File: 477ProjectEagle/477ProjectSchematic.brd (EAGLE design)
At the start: 101.6 x 76.2 mm, 67 parts, among them J1 POWER_JACK_BAT, J2 POWER_JACK_12VOUT, Q1 AO4419, X1 22-23-2051, X10 22-23-2041, X2 XRJK-S-01-6-6-0-2G2-NO

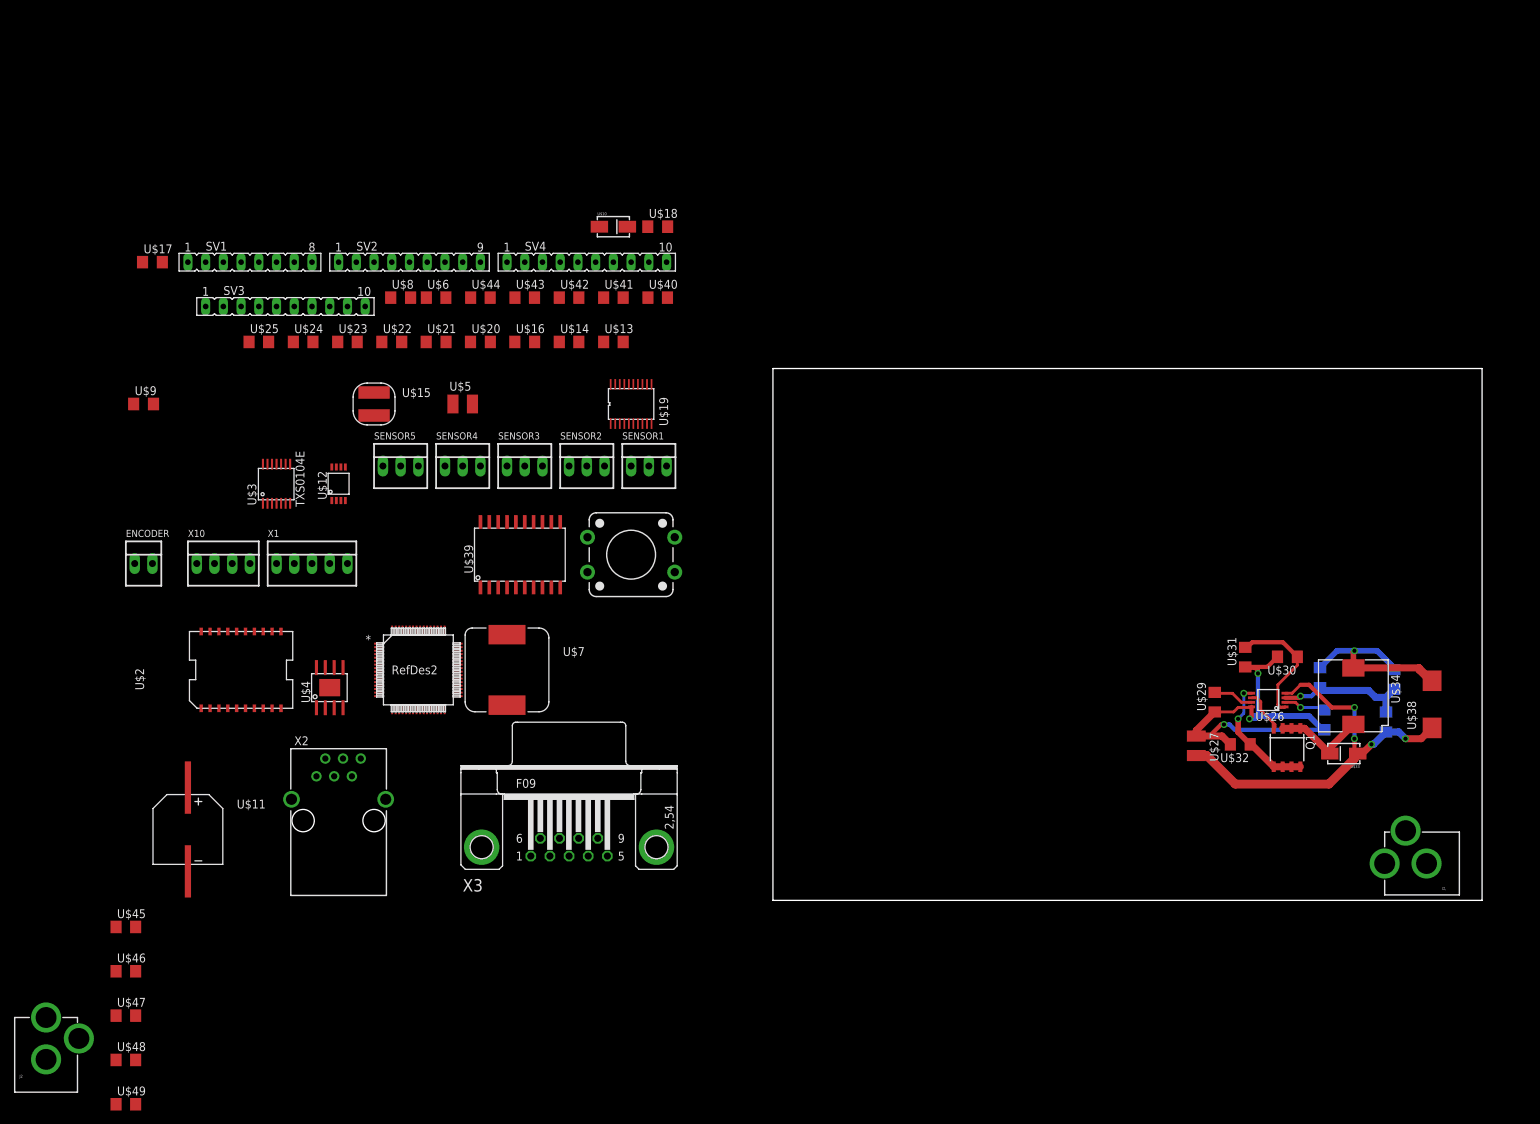
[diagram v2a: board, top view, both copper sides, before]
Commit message: More work on main PCB
Fixed some trace sizes on 12V power supply. Fixed some library
components to be the right size (Cout for the 7V power supply). Started
laying out 7V power supply circuit
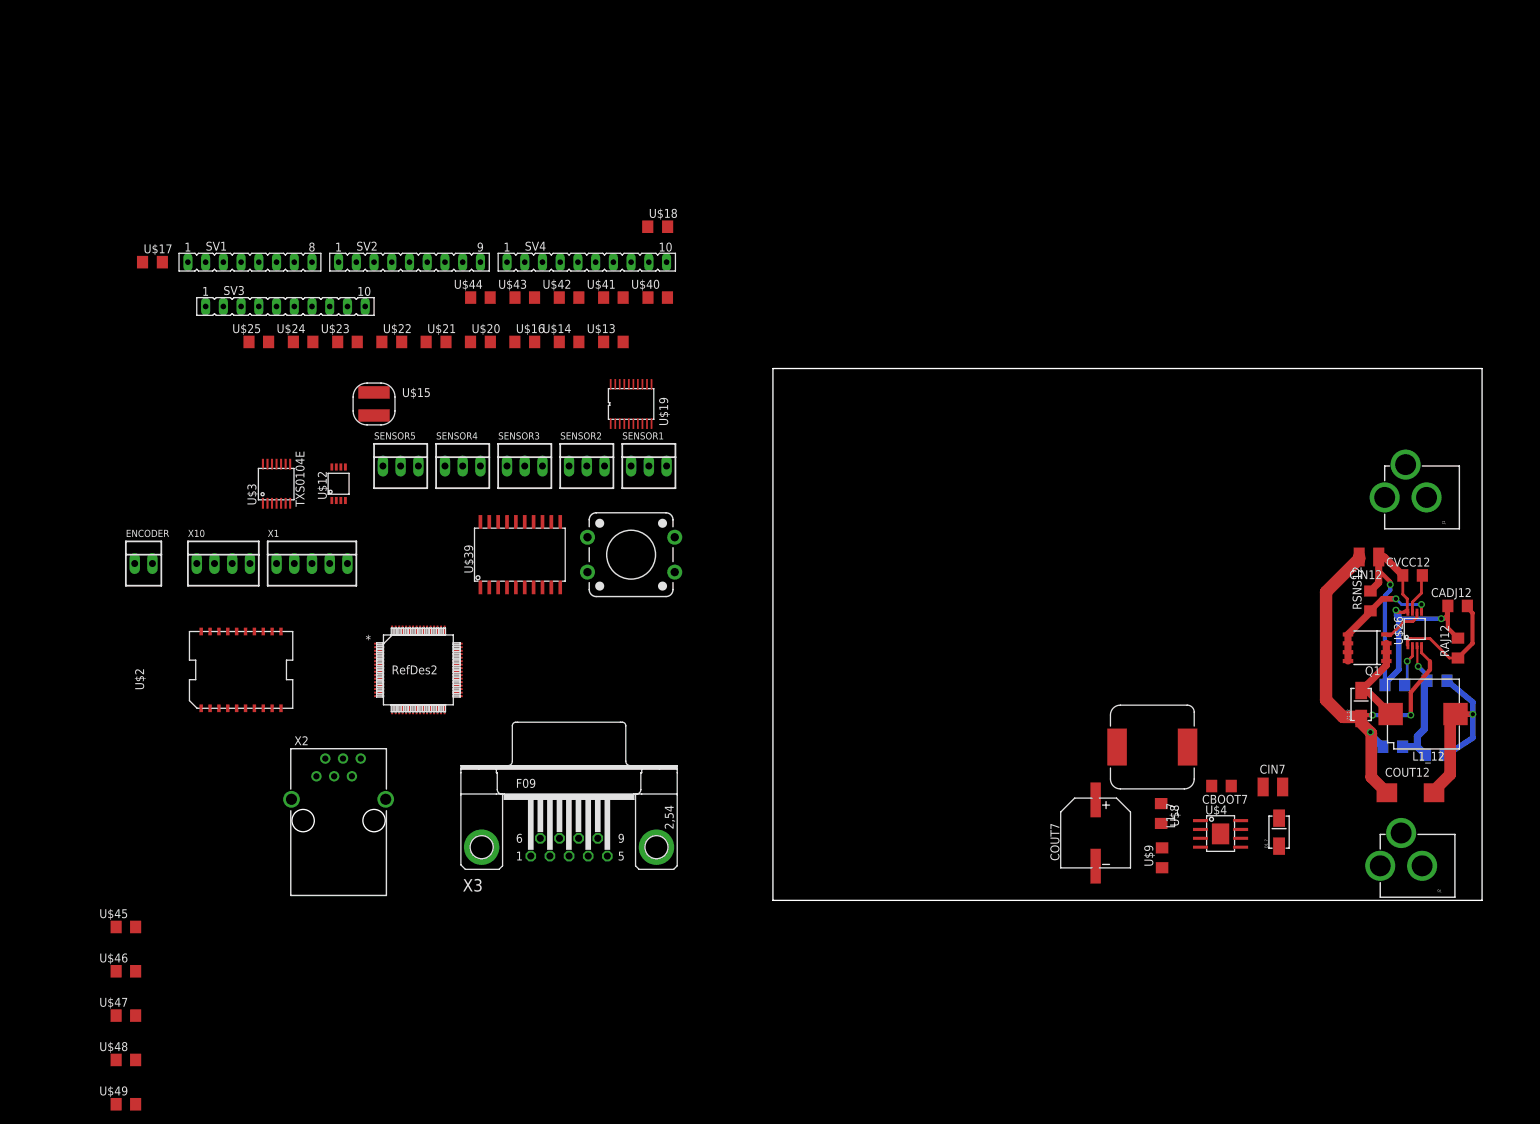
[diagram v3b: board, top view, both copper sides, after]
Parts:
- removed U$10, U$33: B340A-13-F, MinotaurParts:SMA-DIODE
- removed U$11: 270uF, MinotaurParts:CAPSMT_62_J80
- removed U$27, U$5: 10uF, MinotaurParts:C1210
- removed U$28: 110k, MinotaurParts:R1206
- removed U$29: 740nF, MinotaurParts:C1206
- removed U$30: 2.55k, MinotaurParts:R1206
- removed U$31: 1.0nF, MinotaurParts:C1206
- removed U$32: 0.020, MinotaurParts:R1206
- removed U$34: 4.7uH, MinotaurParts:SLF10165
- removed U$38: 33uF, MinotaurParts:D/7343-31W
- removed U$6: 10nF, MinotaurParts:C1206
- removed U$7: 12uH, MinotaurParts:SRR1210
- added CADJ12: 1.0nF, MinotaurParts:C1206
- added CBOOT7: 10nF, MinotaurParts:C1206
- added CIN12, CIN7: 10uF, MinotaurParts:C1210
- added COUT12: 33uF, MinotaurParts:D/7343-31W
- added COUT7: 270uF, MinotaurParts:CAPSMT_62_J80
- added CVCC12: 740nF, MinotaurParts:C1206
- added D1_12, D1_7: B340A-13-F, MinotaurParts:SMA-DIODE
- added L1_12: 4.7uH, MinotaurParts:SLF10165
- added L1_7: 12uH, MinotaurParts:SRR1210
- added RAJ12: 2.55k, MinotaurParts:R1206
- added RSNS12: 0.020, MinotaurParts:R1206
- added RT12: 110k, MinotaurParts:R1206
- moved J2 207.9 mm to (100.7, 4.95), turned to 90 degrees
- moved U$9 159.8 mm to (55.8, 6.10), turned to 90 degrees
- moved U$8 131.7 mm to (55.6, 12.4), turned to 270 degrees
- moved U$4 129.3 mm to (64.1, 9.53), turned to 270 degrees
- moved J1 52.5 mm to (101.3, 57.7)
- moved U$26 23.3 mm to (91.9, 38.9), turned to 0 degrees
- moved Q1 18.3 mm to (85.1, 36.2), turned to 90 degrees
- moved U$36 16.8 mm to (95.1, 31.5), turned to 180 degrees
- moved U$35 12.3 mm to (94.9, 20.9), turned to 0 degrees
- moved U$37 3.66 mm to (88.8, 22.0), turned to 180 degrees
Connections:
- net +12V: now also COUT12.+, L1_12.2; no longer U$34.2, U$38.+
- net +7V: now also COUT7.+, L1_7.B; no longer U$11.+, U$7.B
- net GND: now also CIN12.2, CIN7.2, COUT12.-, COUT7.-, D1_12.-, D1_7.-; no longer U$10.-, U$11.-, U$27.2, U$33.-, U$38.-, U$5.2
- net N$16: now also CBOOT7.1, D1_7.+, L1_7.A; no longer U$10.+, U$6.1, U$7.A
- net N$25: now also CBOOT7.2; no longer U$6.2
- net N$33: now also D1_12.+, L1_12.1; no longer U$33.+, U$34.1
- net N$48: now also RT12.1; no longer U$28.1
- net N$51: now also CVCC12.2; no longer U$29.2
- net N$52: now also CADJ12.2, RAJ12.1; no longer U$30.1, U$31.2
- net N$54: now also RSNS12.1; no longer U$32.1
- net N$59: now also SV4.8
- net N$68: now also SV4.9
- net N$69: now also SV4.7
- net N$74: now also SV4.2
- net N$75: now also SV4.1
- net V+: now also CADJ12.1, CIN12.1, CIN7.1, CVCC12.1, RAJ12.2, RSNS12.2, RT12.2; no longer U$27.1, U$28.2, U$29.1, U$30.2, U$31.1, U$32.2, U$5.1
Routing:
- net GND: track 59.5 -> 62.9 mm, vias 4 -> 3
- net N$50: track 0.00 -> 0.74 mm

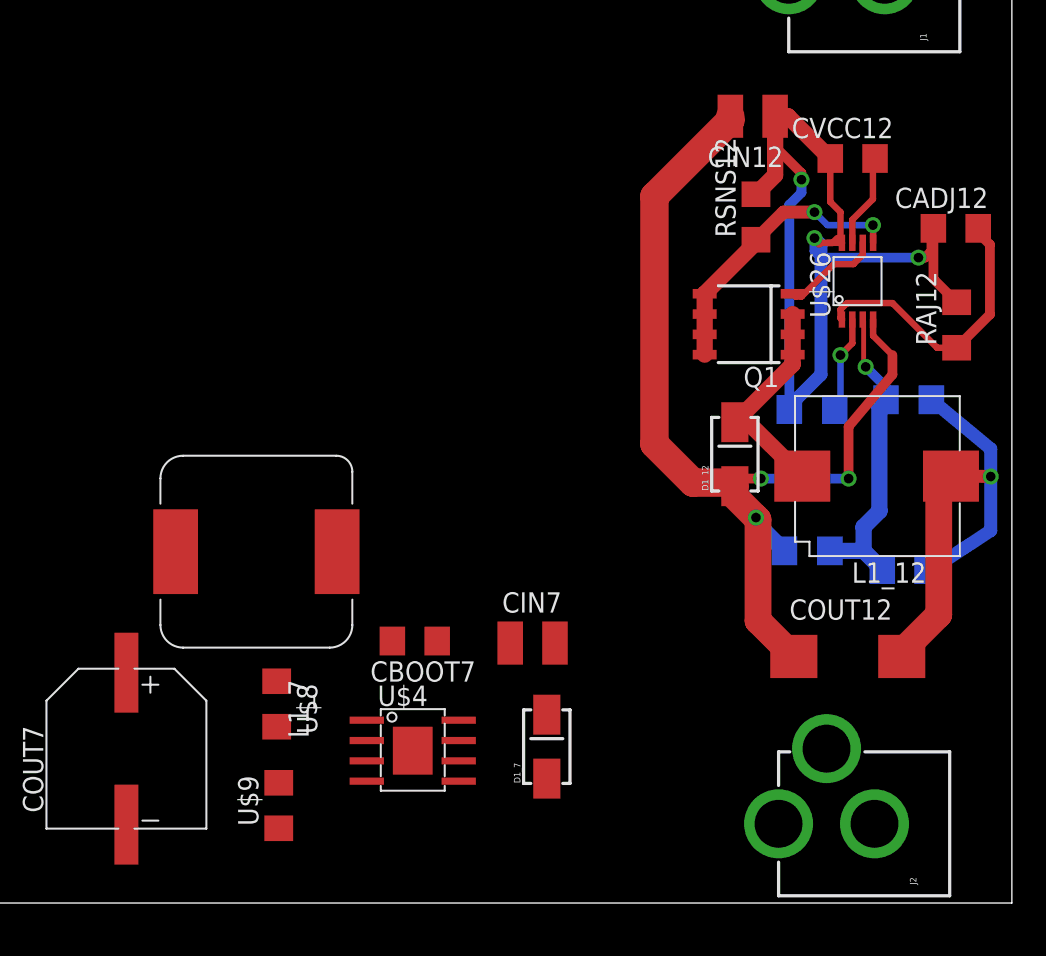
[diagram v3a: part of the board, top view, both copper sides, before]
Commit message: Main PCB - started on 7V power supply
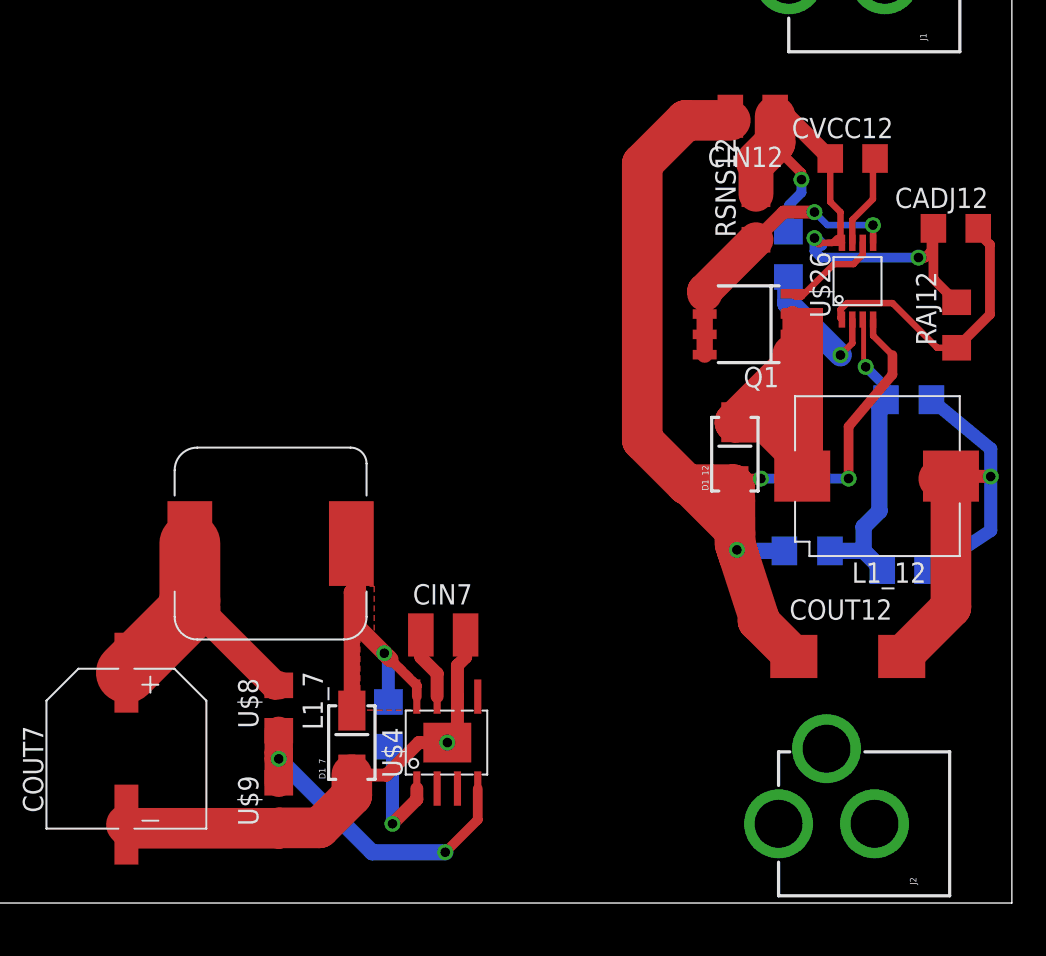
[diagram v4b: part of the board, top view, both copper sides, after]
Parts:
- moved D1_7 12.2 mm to (60.3, 10.0)
- moved RT12 9.81 mm to (87.6, 40.6), turned to 90 degrees
- moved CIN7 5.61 mm to (66.0, 16.8)
- moved CBOOT7 5.46 mm to (62.6, 11.2), flipped to the bottom, turned to 270 degrees
- moved U$4 2.22 mm to (66.3, 10.0), turned to 0 degrees
- moved L1_7 1.02 mm to (55.2, 22.5)
- moved U$8 0.28 mm to (55.8, 12.2), turned to 90 degrees
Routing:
- net GND: track 62.9 -> 100.2 mm, vias 3 -> 4
- net N$16: track 0.00 -> 22.4 mm, vias 0 -> 1
- net N$28: track 0.00 -> 20.9 mm, vias 0 -> 2
- net V+: track 62.0 -> 44.0 mm
- net +7V: track 0.00 -> 17.5 mm
- net N$25: track 0.00 -> 7.76 mm, vias 0 -> 1
- net N$48: track 6.08 -> 8.75 mm
- net +12V: track 30.0 -> 31.4 mm
- net N$33: track 13.9 -> 14.7 mm
- added copper zone on layer 1, net N$16
